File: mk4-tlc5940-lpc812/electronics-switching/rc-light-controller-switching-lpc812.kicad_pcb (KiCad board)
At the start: 2 copper layers, 44 x 23 mm, 20 parts, among them J1 Conn_02x17_Odd_Even, J2 Conn_01x06, J3 Conn_01x06, T1 NMOSSOT23, T2 NMOSSOT23, T3 NMOSSOT23, T4 NMOSSOT23, T5 NMOSSOT23, T6 NMOSSOT23, T7 NMOSSOT23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

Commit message: Tweak schematics, layout text and add BOM CSV files
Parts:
- J1: value Conn_02x17_Odd_Even -> Pinheader right-angle 2x17
- J2, J3: value Conn_01x06 -> Pinheader straight 1x06
- T1, T2, T3, T4, T5, T6, T7, T8, T9: value NMOSSOT23 -> PMV30UN
- U2: value 3V3 -> MCP1703A-3302_SOT23

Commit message: Swap VIN and LED+, add version detection
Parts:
- moved T9 3.72 mm to (170.6, 102.3), turned to 270 degrees
- moved C1 1.02 mm to (164.7, 108.7), turned to 0 degrees
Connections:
- net /OUT8 renamed /OUT15S
- J3 pad 5: /VIN -> /LED+
- J3 pad 6: /LED+ -> /VIN
- U1 pad 20: (no net) -> GND
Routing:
- net /VIN: track 61.4 -> 87.4 mm
- net /OUT-ISP-out: track 51.9 -> 46.3 mm
- net Net-(J1-Pad2): track 6.32 -> 11.9 mm
- net /OUT15S: track 22.2 -> 19.2 mm
- net GND: vias 11 -> 13

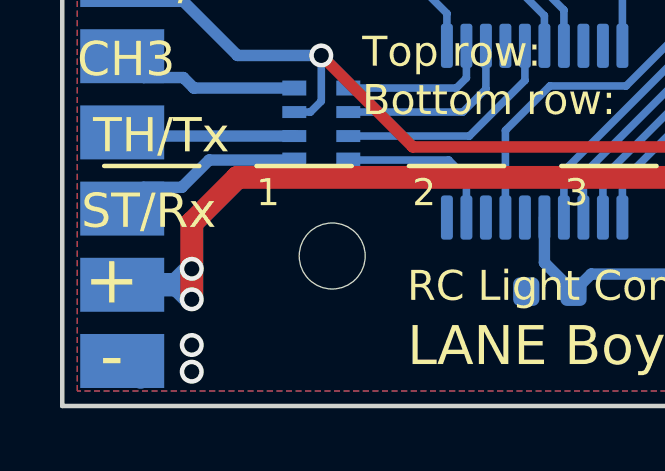
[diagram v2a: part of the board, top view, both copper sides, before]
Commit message: Add more dimensions; Add supply voltage on silk screen
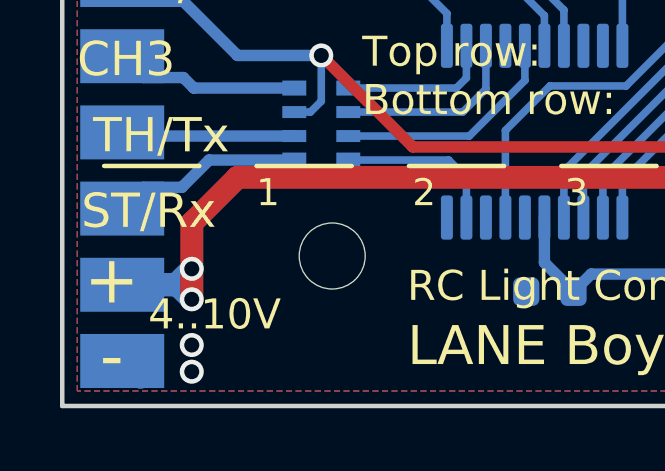
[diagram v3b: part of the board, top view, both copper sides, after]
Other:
- board text added: "4..10V"
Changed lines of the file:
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@@
   (general
     (thickness 1.6)
-    (drawings 41)
+    (drawings 46)
     (tracks 166)
     (zones 0)
@@
     (32 B.Adhes user hide)
     (33 F.Adhes user hide)
-    (34 B.Paste user hide)
+    (34 B.Paste user)
     (35 F.Paste user hide)
     (36 B.SilkS user)
@@
     (39 F.Mask user hide)
     (40 Dwgs.User user hide)
-    (41 Cmts.User user hide)
+    (41 Cmts.User user)
     (42 Eco1.User user hide)
     (43 Eco2.User user hide)
     (44 Edge.Cuts user)
     (45 Margin user)
-    (46 B.CrtYd user hide)
+    (46 B.CrtYd user)
     (47 F.CrtYd user)
-    (48 B.Fab user hide)
-    (49 F.Fab user hide)
+    (48 B.Fab user)
+    (49 F.Fab user)
   )
   (setup
-    (last_trace_width 0.762)
+    (last_trace_width 0.254)
     (user_trace_width 0.2032)
     (user_trace_width 0.381)
@@
     )
   )
+  (gr_text 4..10V (at 140.08 110.952) (layer F.SilkS)
+    (effects (font (size 1 1) (thickness 0.2)))
+  )
+  (dimension 5 (width 0.15) (layer Cmts.User)
+    (gr_text "5.000 mm" (at 131.7 111.5 90) (layer Cmts.User)
+      (effects (font (size 1 1) (thickness 0.15)))
+    )
+    (feature1 (pts (xy 144 109) (xy 132.413579 109)))
+    (feature2 (pts (xy 144 114) (xy 132.413579 114)))
+    (crossbar (pts (xy 133 114) (xy 133 109)))
+    (arrow1a (pts (xy 133 109) (xy 133.586421 110.126504)))
+    (arrow1b (pts (xy 133 109) (xy 132.413579 110.126504)))
+    (arrow2a (pts (xy 133 114) (xy 133.586421 112.873496)))
+    (arrow2b (pts (xy 133 114) (xy 132.413579 112.873496)))
+  )
+  (dimension 35 (width 0.15) (layer Cmts.User)
+    (gr_text "35.000 mm" (at 152.5 120.3) (layer Cmts.User)
+      (effects (font (size 1 1) (thickness 0.15)))
+    )
+    (feature1 (pts (xy 170 109) (xy 170 119.586421)))
+    (feature2 (pts (xy 135 109) (xy 135 119.586421)))
+    (crossbar (pts (xy 135 119) (xy 170 119)))
+    (arrow1a (pts (xy 170 119) (xy 168.873496 119.586421)))
+    (arrow1b (pts (xy 170 119) (xy 168.873496 118.413579)))
+    (arrow2a (pts (xy 135 119) (xy 136.126504 119.586421)))
+    (arrow2b (pts (xy 135 119) (xy 136.126504 118.413579)))
+  )
+  (dimension 9 (width 0.15) (layer Cmts.User)
+    (gr_text "9.000 mm" (at 174.5 117.3) (layer Cmts.User)
+      (effects (font (size 1 1) (thickness 0.15)))
+    )
+    (feature1 (pts (xy 179 109) (xy 179 116.586421)))
+    (feature2 (pts (xy 170 109) (xy 170 116.586421)))
+    (crossbar (pts (xy 170 116) (xy 179 116)))
+    (arrow1a (pts (xy 179 116) (xy 177.873496 116.586421)))
+    (arrow1b (pts (xy 179 116) (xy 177.873496 115.413579)))
+    (arrow2a (pts (xy 170 116) (xy 171.126504 116.586421)))
+    (arrow2b (pts (xy 170 116) (xy 171.126504 115.413579)))
+  )
+  (dimension 9 (width 0.15) (layer Cmts.User)
+    (gr_text "9.000 mm" (at 139.5 117.3) (layer Cmts.User)
+      (effects (font (size 1 1) (thickness 0.15)))
+    )
+    (feature1 (pts (xy 144 109) (xy 144 116.586421)))
+    (feature2 (pts (xy 135 109) (xy 135 116.586421)))
+    (crossbar (pts (xy 135 116) (xy 144 116)))
+    (arrow1a (pts (xy 144 116) (xy 142.873496 116.586421)))
+    (arrow1b (pts (xy 144 116) (xy 142.873496 115.413579)))
+    (arrow2a (pts (xy 135 116) (xy 136.126504 116.586421)))
+    (arrow2b (pts (xy 135 116) (xy 136.126504 115.413579)))
+  )
   (gr_text "Top row:\nBottom row:" (at 145 103) (layer F.SilkS)
     (effects (font (size 1 1) (thickness 0.2)) (justify left))
@@
   (gr_line (start 159.892 105.999) (end 156.717 106) (layer F.SilkS) (width 0.15))
   (dimension 15 (width 0.15) (layer Cmts.User)
-    (gr_text "15.000 mm" (at 170.3 106.5 90) (layer Cmts.User)
+    (gr_text "15.000 mm" (at 127.7 106.5 90) (layer Cmts.User)
       (effects (font (size 1 1) (thickness 0.15)))
     )
-    (feature1 (pts (xy 169 99) (xy 169.586421 99)))
-    (feature2 (pts (xy 169 114) (xy 169.586421 114)))
-    (crossbar (pts (xy 169 114) (xy 169 99)))
-    (arrow1a (pts (xy 169 99) (xy 169.586421 100.126504)))
-    (arrow1b (pts (xy 169 99) (xy 168.413579 100.126504)))
-    (arrow2a (pts (xy 169 114) (xy 169.586421 112.873496)))
-    (arrow2b (pts (xy 169 114) (xy 168.413579 112.873496)))
+    (feature1 (pts (xy 135 99) (xy 128.413579 99)))
+    (feature2 (pts (xy 135 114) (xy 128.413579 114)))
+    (crossbar (pts (xy 129 114) (xy 129 99)))
+    (arrow1a (pts (xy 129 99) (xy 129.586421 100.126504)))
+    (arrow1b (pts (xy 129 99) (xy 128.413579 100.126504)))
+    (arrow2a (pts (xy 129 114) (xy 129.586421 112.873496)))
+    (arrow2b (pts (xy 129 114) (xy 128.413579 112.873496)))
   )
   (gr_text JLCJLCJLCJLC (at 174.37 112.776) (layer B.SilkS)
@@
   )
   (dimension 44 (width 0.3) (layer Cmts.User)
-    (gr_text "44.000 mm" (at 157 118.1) (layer Cmts.User)
+    (gr_text "44.000 mm" (at 157 124.1) (layer Cmts.User)
       (effects (font (size 1.5 1.5) (thickness 0.3)))
     )
-    (feature1 (pts (xy 179 114) (xy 179 116.586421)))
-    (feature2 (pts (xy 135 114) (xy 135 116.586421)))
-    (crossbar (pts (xy 135 116) (xy 179 116)))
-    (arrow1a (pts (xy 179 116) (xy 177.873496 116.586421)))
-    (arrow1b (pts (xy 179 116) (xy 177.873496 115.413579)))
-    (arrow2a (pts (xy 135 116) (xy 136.126504 116.586421)))
-    (arrow2b (pts (xy 135 116) (xy 136.126504 115.413579)))
+    (feature1 (pts (xy 179 114) (xy 179 122.586421)))
+    (feature2 (pts (xy 135 114) (xy 135 122.586421)))
+    (crossbar (pts (xy 135 122) (xy 179 122)))
+    (arrow1a (pts (xy 179 122) (xy 177.873496 122.586421)))
+    (arrow1b (pts (xy 179 122) (xy 177.873496 121.413579)))
+    (arrow2a (pts (xy 135 122) (xy 136.126504 122.586421)))
+    (arrow2b (pts (xy 135 122) (xy 136.126504 121.413579)))
   )
   (gr_text Rev1 (at 146.073929 112.349) (layer B.SilkS)
@@
   )
   (zone (net 2) (net_name GND) (layer Top) (hatch edge 0.508)
-    (connect_pads (clearance 0.3048))
+    (connect_pads (clearance 0.254))
     (min_thickness 0.254)
     (fill yes (arc_segments 32) (thermal_gap 0.3556) (thermal_bridge_width 0.3556))
